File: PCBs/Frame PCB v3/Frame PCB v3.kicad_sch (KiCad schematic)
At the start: 16 parts, among them J1 Nichrome 1, J2 Nichrome 2, J3 Battery in, J6 Switch, q1 Voltage regulator

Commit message: updated PCBS
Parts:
- removed J1: Nichrome 1, Connector_JST:JST_XH_B3B-XH-A_1x03_P2.50mm_Vertical, symbol Connector:Conn_01x03_Socket
- removed J2: Nichrome 2, Connector_JST:JST_XH_B3B-XH-A_1x03_P2.50mm_Vertical, symbol Connector:Conn_01x03_Socket
- removed VehiclePowerOn1: I2C Connector, Connector_JST:JST_XH_B4B-XH-A_1x04_P2.50mm_Vertical, symbol Connector:Conn_01x04_Socket
- added J10, J11: Nichrome, Connector_JST:JST_XH_B2B-XH-A_1x02_P2.50mm_Vertical, symbol Connector:Conn_01x02_Socket
- added J5: BayConnector, Connector_JST:JST_XH_B4B-XH-A_1x04_P2.50mm_Vertical, symbol Connector:Conn_01x04_Socket
- added Q5, Q6: Nichrome, Package_TO_SOT_THT:TO-220-3_Vertical, symbol Transistor_FET:IRLZ44N
- renumbered SensorBoard1 to J4
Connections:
- net +5V: now also Q5.3 (S), Q6.3 (S)
- net GND: now also J10.1 (Pin_1), J11.1 (Pin_1), J5.1 (Pin_1)
- net Nichrome1: now also Q5.1 (G)
- net Nichrome2: now also Q6.1 (G)
- net VehicleRX: now also J5.3 (Pin_3)
- net VehicleTX: now also J5.2 (Pin_2)
- net VehicleOn: now reaches Teensy4.1.5 (PWM)
- net VehicleOn: now also J5.4 (Pin_4)
- net VehicleSwitch: no longer names the net of Teensy4.1.32 (A17)
- new net: J11.2 (Pin_2), Q6.2 (D)
- new net: J10.2 (Pin_2), Q5.2 (D)

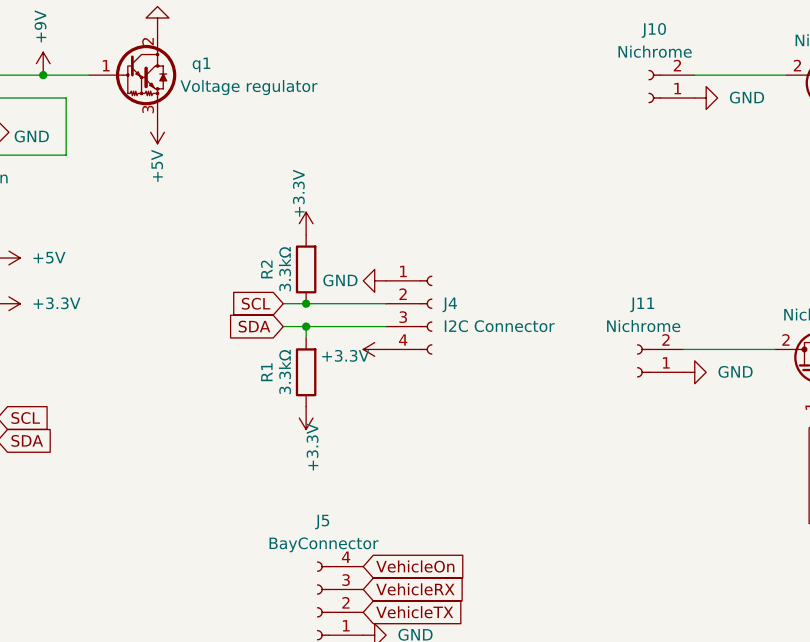
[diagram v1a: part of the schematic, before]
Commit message: updated pcb hole spacing
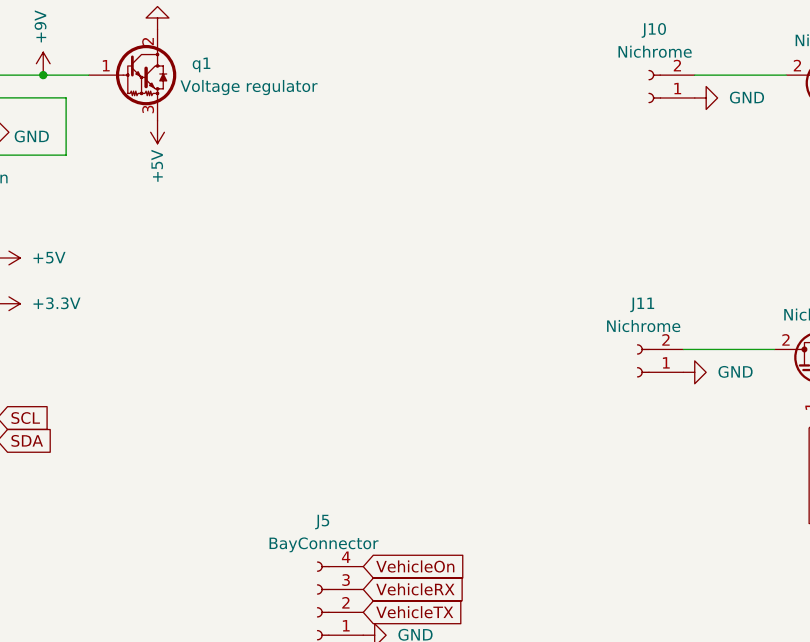
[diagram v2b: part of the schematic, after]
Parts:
- removed J4: I2C Connector, Connector_JST:JST_XH_B4B-XH-A_1x04_P2.50mm_Vertical, symbol Connector:Conn_01x04_Socket
- removed R1, R2: 3.3kΩ, Resistor_SMD:R_0805_2012Metric_Pad1.20x1.40mm_HandSolder, symbol Device:R
